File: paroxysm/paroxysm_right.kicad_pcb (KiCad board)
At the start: 2 copper layers, 117.5 x 89.9 mm, 19 parts, among them SW10 SW_Push, SW11 SW_Push, SW12 SW_Push, SW14 SW_Push, SW15 SW_Push, SW16 SW_Push, SW17 SW_Push, SW18 SW_Push, SW20 SW_Push, SW21 SW_Push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

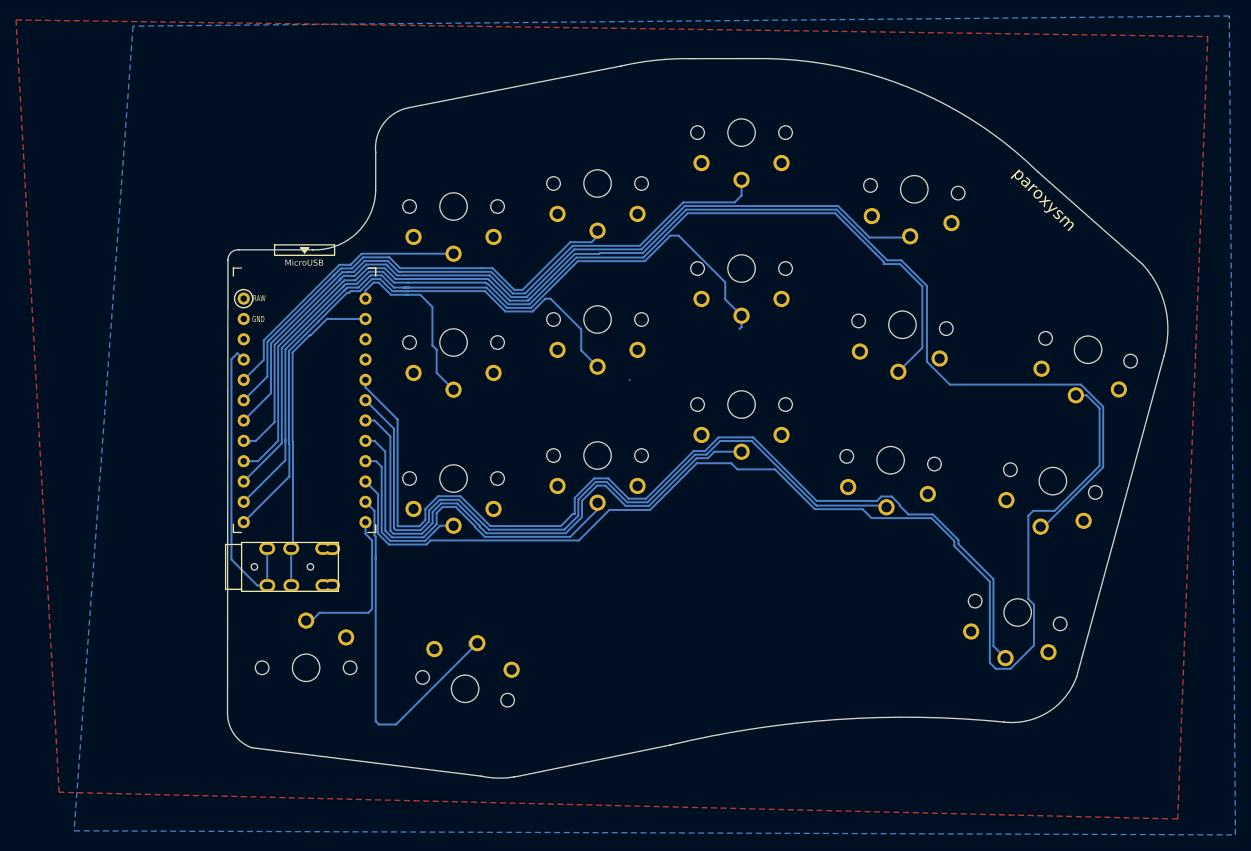
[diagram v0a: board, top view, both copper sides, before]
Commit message: Add original and one sided copies of paroxysm
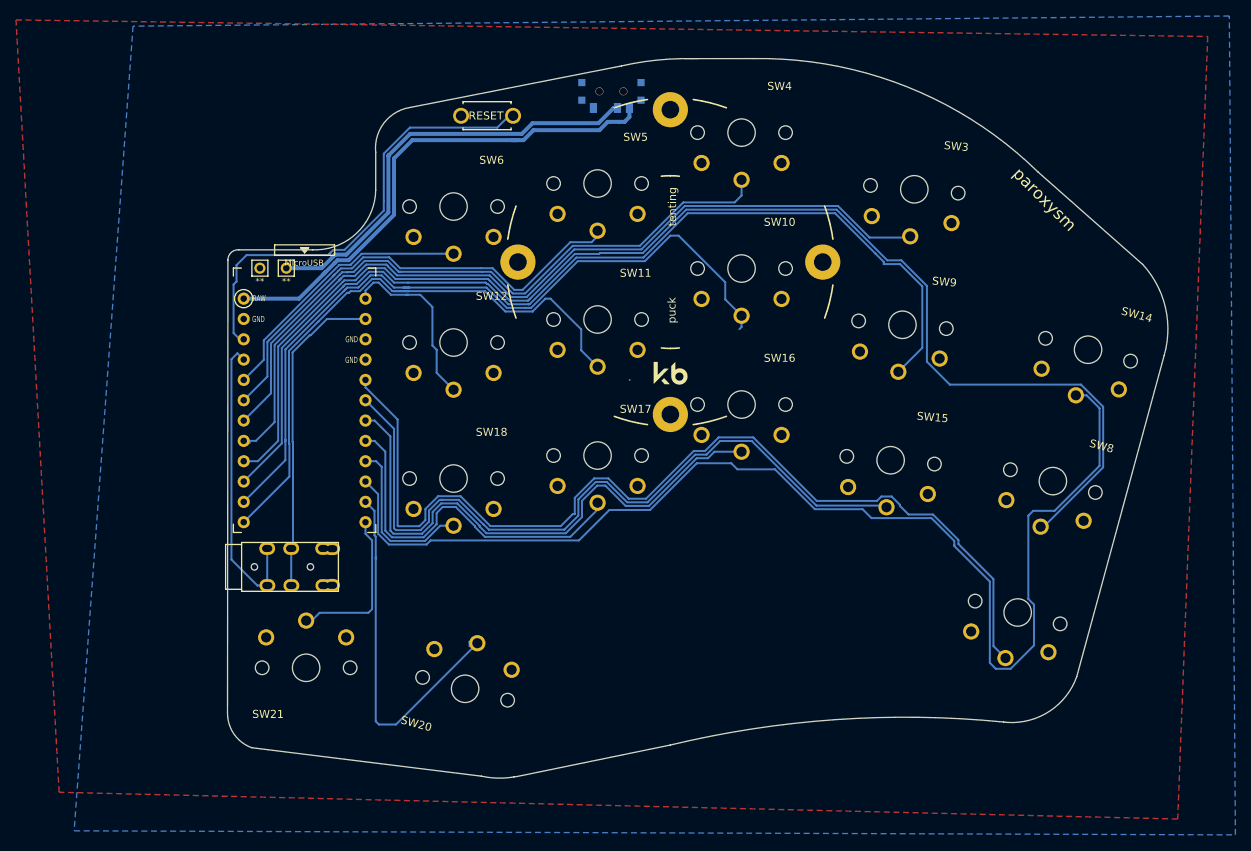
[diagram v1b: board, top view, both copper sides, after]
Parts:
- added **: Val**, kbd:1pin_conn, B.Cu at (38.4, 48.8)
- added BatGND1: MountingHole_Pad, kbd:1pin_conn, B.Cu at (35.1, 48.8)
- added REF**: Tenting Puck, kbd:Tenting_Puck2, B.Cu at (86.4, 48.0)
- added RSW1: SW_Push, kbd:ResetSW, B.Cu at (63.4, 29.7)
- added SW_POWER1: SW_SPDT, Kailh:SPDT_C128955, B.Cu at (79.0, 26.7)
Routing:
- net raw: track 0.00 -> 63.9 mm
- net reset: track 0.50 -> 56.9 mm
- net BT+: track 0.00 -> 54.0 mm
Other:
- board text added: "15°"
- board text added: "16mm"
- board text added: "2.7mm"
- board text added: "5°"
- board text added: "6.3mm"
- board text added: "6mm"

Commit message: Simplified paroxysm_right, update README
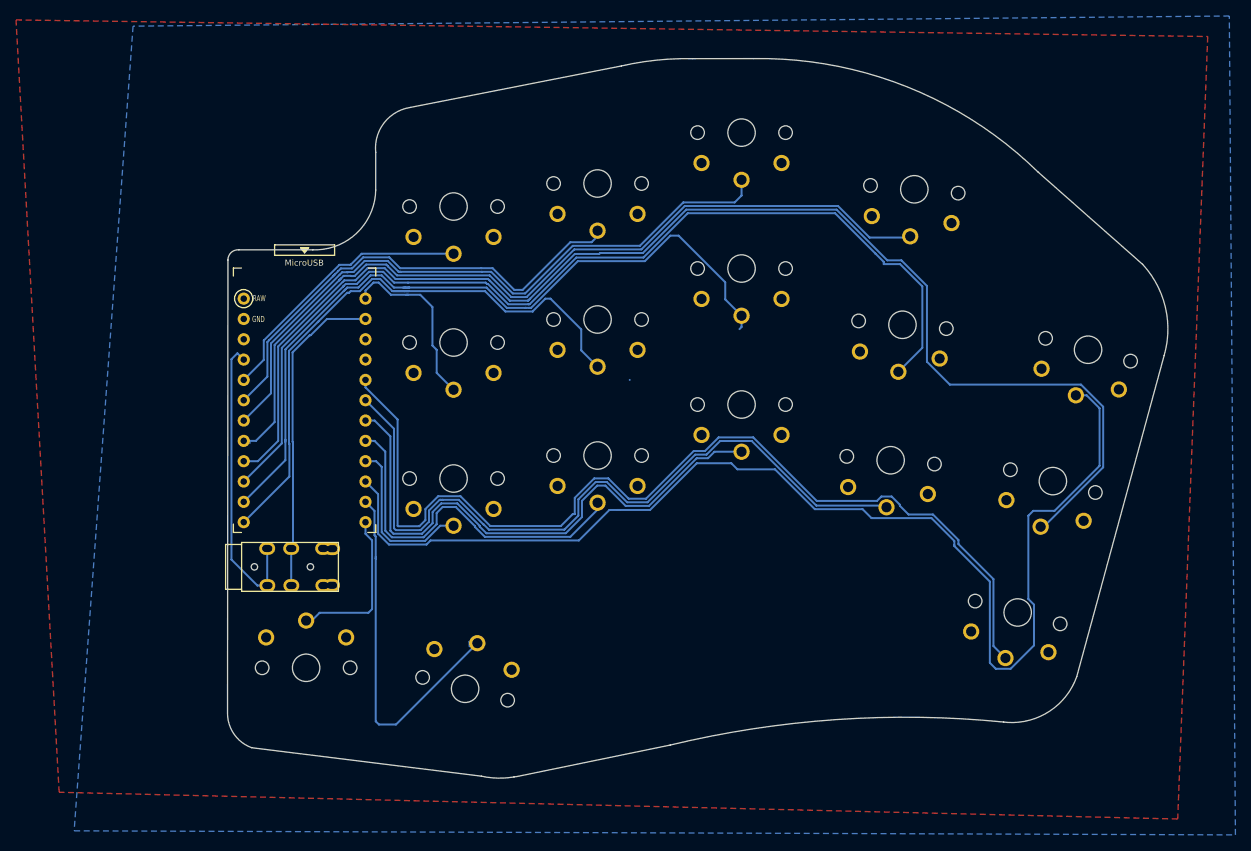
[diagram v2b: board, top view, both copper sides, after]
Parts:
- removed **: Val**, kbd:1pin_conn
- removed BatGND1: MountingHole_Pad, kbd:1pin_conn
- removed REF**: Tenting Puck, kbd:Tenting_Puck2
- removed RSW1: SW_Push, kbd:ResetSW
- removed SW_POWER1: SW_SPDT, Kailh:SPDT_C128955
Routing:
- net raw: track 63.9 -> 0.00 mm
- net reset: track 56.9 -> 0.50 mm
- net BT+: track 54.0 -> 0.00 mm
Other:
- board text removed: "15°"
- board text removed: "16mm"
- board text removed: "2.7mm"
- board text removed: "5°"
- board text removed: "6.3mm"
- board text removed: "6mm"
- board text removed: "paroxysm"
